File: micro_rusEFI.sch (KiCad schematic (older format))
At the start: 53 parts, among them J12 Conn_01x01, J13 Conn_01x01, J3 Conn_01x01, J4 Conn_02x05_Counter_Clockwise, J5 Conn_01x01, U3 molex_48pin_MRE, U7 XC6206 3.3V

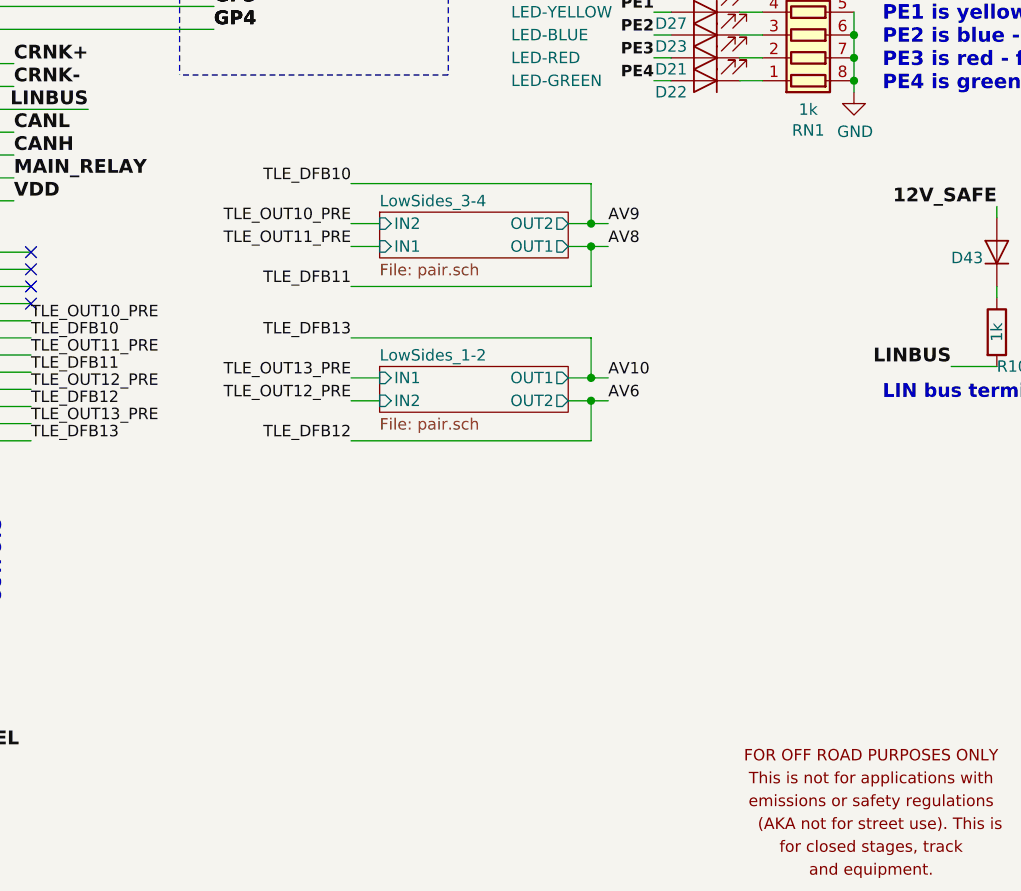
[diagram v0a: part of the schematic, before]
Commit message: AV6, AV8, AV9 and AV10 can now direct drive the digital outputs.
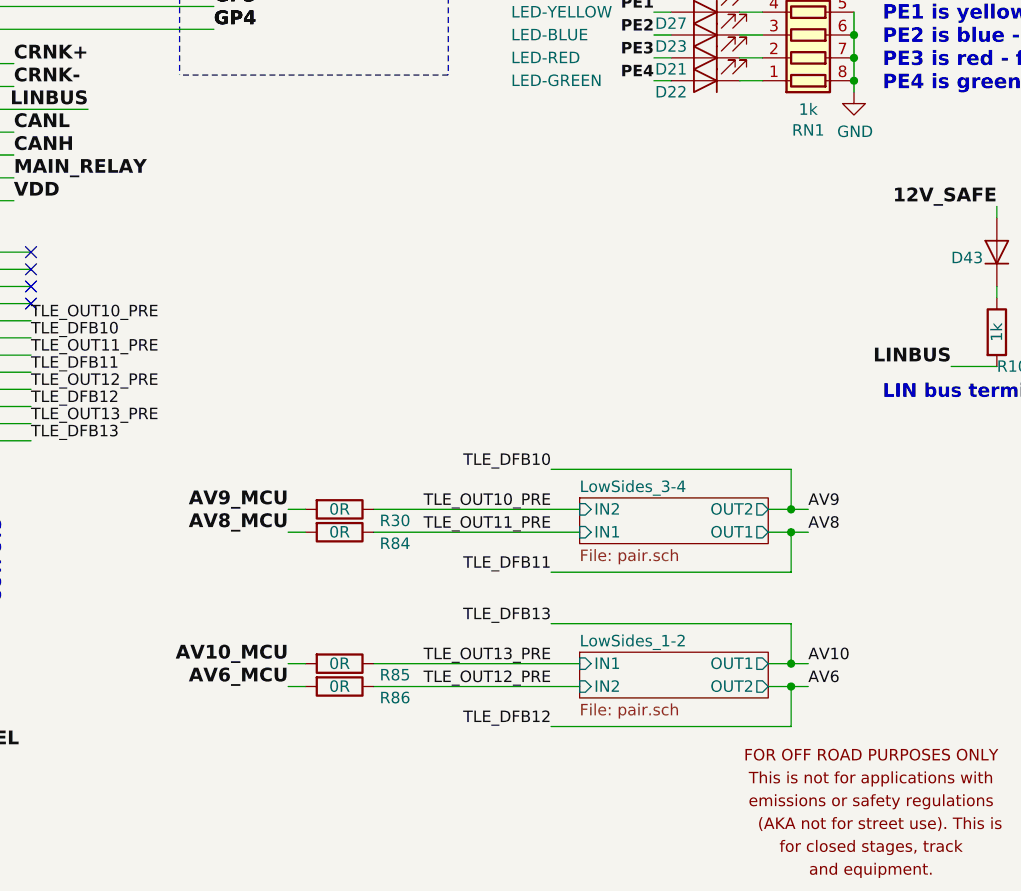
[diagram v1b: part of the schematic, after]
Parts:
- added R30, R84, R85: 0R, Resistor_SMD:R_0603_1608Metric, symbol Device:R
- added R86: 0R, Resistor_SMD:R_0805_2012Metric, symbol Device:R
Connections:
- net AV10_MCU: now also R85.2
- net AV6_MCU: now also R86.2
- net AV8_MCU: now also R84.2
- net AV9_MCU: now also R30.2
- net TLE_OUT10_PRE: now also R30.1
- net TLE_OUT11_PRE: now also R84.1
- net TLE_OUT12_PRE: now also R86.1
- net TLE_OUT13_PRE: now also R85.1
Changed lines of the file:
@@
 $EndComp
 $Sheet
-S 12450 6725 825  200
+S 13325 7975 825  200
 U 5E8F2073
 F0 "LowSides_3-4" 50
 F1 "pair.sch" 50
-F2 "IN1" I L 12450 6875 50
-F3 "IN2" I L 12450 6775 50
-F4 "OUT1" O R 13275 6875 50
-F5 "OUT2" O R 13275 6775 50
+F2 "IN1" I L 13325 8125 50
+F3 "IN2" I L 13325 8025 50
+F4 "OUT1" O R 14150 8125 50
+F5 "OUT2" O R 14150 8025 50
 $EndSheet
 $Sheet
-S 12450 7400 825  200
+S 13325 8650 825  200
 U 5E8F1149
 F0 "LowSides_1-2" 50
 F1 "pair.sch" 50
-F2 "IN1" I L 12450 7450 50
-F3 "IN2" I L 12450 7550 50
-F4 "OUT1" O R 13275 7450 50
-F5 "OUT2" O R 13275 7550 50
+F2 "IN1" I L 13325 8700 50
+F3 "IN2" I L 13325 8800 50
+F4 "OUT1" O R 14150 8700 50
+F5 "OUT2" O R 14150 8800 50
 $EndSheet
 Wire Wire Line
@@
 Wire Wire Line
 	10750 7500 10925 7500
-Text Label 12325 7550 2    50   ~ 0
+Text Label 13200 8800 2    50   ~ 0
 TLE_OUT12_PRE
 Text Label 8875 3400 2    50   ~ 0
@@
 Text Label 8875 3700 2    50   ~ 0
 PD15
-Wire Wire Line
-	12325 7550 12450 7550
-Wire Wire Line
-	12450 7450 12325 7450
-Wire Wire Line
-	12325 6775 12450 6775
-Wire Wire Line
-	12325 6875 12450 6875
 Wire Wire Line
 	7900 1650 7900 1575
@@
 Text Label 3425 4425 2    60   ~ 12
 AV6
-Text Label 13450 6775 0    50   ~ 0
+Text Label 14325 8025 0    50   ~ 0
 AV9
-Text Label 13450 6875 0    50   ~ 0
+Text Label 14325 8125 0    50   ~ 0
 AV8
-Text Label 13450 7450 0    50   ~ 0
+Text Label 14325 8700 0    50   ~ 0
 AV10
 Wire Wire Line
@@
 	3425 4725 4050 4725
 Wire Wire Line
-	13275 7450 13375 7450
-Wire Wire Line
-	13275 7550 13375 7550
-Wire Wire Line
-	13275 6775 13375 6775
-Wire Wire Line
-	13275 6875 13375 6875
+	14150 8700 14250 8700
+Wire Wire Line
+	14150 8800 14250 8800
+Wire Wire Line
+	14150 8025 14250 8025
+Wire Wire Line
+	14150 8125 14250 8125
 Wire Wire Line
 	10750 6975 10925 6975
 Wire Wire Line
-	12325 7725 13375 7725
-Wire Wire Line
-	13375 7725 13375 7550
-Connection ~ 13375 7550
-Wire Wire Line
-	13375 7550 13450 7550
-Text Label 13450 7550 0    50   ~ 0
+	13200 8975 14250 8975
+Wire Wire Line
+	14250 8975 14250 8800
+Connection ~ 14250 8800
+Wire Wire Line
+	14250 8800 14325 8800
+Text Label 14325 8800 0    50   ~ 0
 AV6
 Text Label 10925 7275 0    50   ~ 0
@@
 Wire Wire Line
 	10750 7725 10925 7725
-Text Label 12325 7725 2    50   ~ 0
+Text Label 13200 8975 2    50   ~ 0
 TLE_DFB12
 Wire Wire Line
-	12325 7275 13375 7275
-Wire Wire Line
-	13375 7275 13375 7450
-Connection ~ 13375 7450
-Wire Wire Line
-	13375 7450 13450 7450
-Wire Wire Line
-	12325 6600 13375 6600
-Wire Wire Line
-	13375 6600 13375 6775
-Connection ~ 13375 6775
-Wire Wire Line
-	13375 6775 13450 6775
-Wire Wire Line
-	12325 7050 13375 7050
-Wire Wire Line
-	13375 7050 13375 6875
-Connection ~ 13375 6875
-Wire Wire Line
-	13375 6875 13450 6875
-Text Label 12325 7275 2    50   ~ 0
+	13200 8525 14250 8525
+Wire Wire Line
+	14250 8525 14250 8700
+Connection ~ 14250 8700
+Wire Wire Line
+	14250 8700 14325 8700
+Wire Wire Line
+	13200 7850 14250 7850
+Wire Wire Line
+	14250 7850 14250 8025
+Connection ~ 14250 8025
+Wire Wire Line
+	14250 8025 14325 8025
+Wire Wire Line
+	13200 8300 14250 8300
+Wire Wire Line
+	14250 8300 14250 8125
+Connection ~ 14250 8125
+Wire Wire Line
+	14250 8125 14325 8125
+Text Label 13200 8525 2    50   ~ 0
 TLE_DFB13
-Text Label 12325 7450 2    50   ~ 0
+Text Label 13200 8700 2    50   ~ 0
 TLE_OUT13_PRE
 Wire Wire Line
@@
 Wire Wire Line
 	10750 7425 10925 7425
-Text Label 12325 6875 2    50   ~ 0
+Text Label 13200 8125 2    50   ~ 0
 TLE_OUT11_PRE
-Text Label 12325 7050 2    50   ~ 0
+Text Label 13200 8300 2    50   ~ 0
 TLE_DFB11
-Text Label 12325 6775 2    50   ~ 0
+Text Label 13200 8025 2    50   ~ 0
 TLE_OUT10_PRE
-Text Label 12325 6600 2    50   ~ 0
+Text Label 13200 7850 2    50   ~ 0
 TLE_DFB10
 Text Label 12125 3525 0    60   ~ 12
@@
 Wire Wire Line
 	6200 5600 6275 5600
+$Comp
+L Device:R R85
+U 1 1 5EE637EC
+P 12275 8700
+F 0 "R85" V 12325 8875 50  0000 L CNN
+F 1 "0R" V 12275 8700 50  0000 C CNN
+F 2 "Resistor_SMD:R_0603_1608Metric" V 12205 8700 50  0001 C CNN
+F 3 "~" H 12275 8700 50  0001 C CNN
+F 4 "Uniroyal Elec" H 3950 2775 50  0001 C CNN "Manufacturer"
+F 5 "0603WAF0000T5E" H 3950 2775 50  0001 C CNN "Part #"
+F 6 "" H 3950 2775 50  0001 C CNN "VEND"
+F 7 "" H 3950 2775 50  0001 C CNN "VEND#"
+F 8 "C21189" H 12275 8700 50  0001 C CNN "LCSC"
+	1    12275 8700
+	0    1    1    0
+$EndComp
+$Comp
+L Device:R R86
+U 1 1 5EEECFE7
+P 12275 8800
+F 0 "R86" V 12325 8975 50  0000 L CNN
+F 1 "0R" V 12275 8800 50  0000 C CNN
+F 2 "Resistor_SMD:R_0805_2012Metric" V 12205 8800 50  0001 C CNN
+F 3 "~" H 12275 8800 50  0001 C CNN
+F 4 "" H 3950 2875 50  0001 C CNN "Manufacturer"
+F 5 "" H 3950 2875 50  0001 C CNN "Part #"
+F 6 "" H 3950 2875 50  0001 C CNN "VEND"
+F 7 "" H 3950 2875 50  0001 C CNN "VEND#"
+F 8 "" H 12275 8800 50  0001 C CNN "LCSC"
+	1    12275 8800
+	0    1    1    0
+$EndComp
+$Comp
+L Device:R R30
+U 1 1 5EF0FADE
+P 12275 8025
+F 0 "R30" V 12325 8200 50  0000 L CNN
+F 1 "0R" V 12275 8025 50  0000 C CNN
+F 2 "Resistor_SMD:R_0603_1608Metric" V 12205 8025 50  0001 C CNN
+F 3 "~" H 12275 8025 50  0001 C CNN
+F 4 "Uniroyal Elec" H 3950 2100 50  0001 C CNN "Manufacturer"
+F 5 "0603WAF0000T5E" H 3950 2100 50  0001 C CNN "Part #"
+F 6 "" H 3950 2100 50  0001 C CNN "VEND"
+F 7 "" H 3950 2100 50  0001 C CNN "VEND#"
+F 8 "C21189" H 12275 8025 50  0001 C CNN "LCSC"
+	1    12275 8025
+	0    1    1    0
+$EndComp
+$Comp
+L Device:R R84
+U 1 1 5EF0FAED
+P 12275 8125
+F 0 "R84" V 12325 8300 50  0000 L CNN
+F 1 "0R" V 12275 8125 50  0000 C CNN
+F 2 "Resistor_SMD:R_0603_1608Metric" V 12205 8125 50  0001 C CNN
+F 3 "~" H 12275 8125 50  0001 C CNN
+F 4 "Uniroyal Elec" H 3950 2200 50  0001 C CNN "Manufacturer"
+F 5 "0603WAF0000T5E" H 3950 2200 50  0001 C CNN "Part #"
+F 6 "" H 3950 2200 50  0001 C CNN "VEND"
+F 7 "" H 3950 2200 50  0001 C CNN "VEND#"
+F 8 "C21189" H 12275 8125 50  0001 C CNN "LCSC"
+	1    12275 8125
+	0    1    1    0
+$EndComp
+Text Label 12050 8025 2    60   ~ 12
+AV9_MCU
+Text Label 12050 8125 2    60   ~ 12
+AV8_MCU
+Text Label 12050 8700 2    60   ~ 12
+AV10_MCU
+Text Label 12050 8800 2    60   ~ 12
+AV6_MCU
+Wire Wire Line
+	12050 8025 12125 8025
+Wire Wire Line
+	12050 8125 12125 8125
+Wire Wire Line
+	12050 8700 12125 8700
+Wire Wire Line
+	12050 8800 12125 8800
+Wire Wire Line
+	12425 8700 13325 8700
+Wire Wire Line
+	12425 8800 13325 8800
+Wire Wire Line
+	12425 8025 13325 8025
+Wire Wire Line
+	12425 8125 13325 8125
 $EndSCHEMATC

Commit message: 0.5.1 released
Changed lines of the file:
@@
 F19 "AV3_MCU" I R 5600 4125 60
 F20 "AV5_MCU" I R 5600 4325 60
-F21 "12V-SWITCH" I L 4050 5150 60
-F22 "Vbat_MCU" I R 5600 5150 60
-F23 "AV6" I L 4050 4425 60
-F24 "AV7" I L 4050 4525 60
-F25 "AV8" I L 4050 4625 60
-F26 "AV9" I L 4050 4725 60
-F27 "AV6_MCU" I R 5600 4425 60
-F28 "AV7_MCU" I R 5600 4525 60
-F29 "AV8_MCU" I R 5600 4625 60
-F30 "AV9_MCU" I R 5600 4725 60
-F31 "CAM" I L 4050 5000 60
-F32 "CAM_MCU" I R 5600 5000 60
-F33 "AV4" I L 4050 4225 60
-F34 "AV4_MCU" I R 5600 4225 60
-F35 "AGND" I R 5600 5400 50
-F36 "AV11_MCU" I R 5600 5275 50
+F21 "Vbat_MCU" I R 5600 5150 60
+F22 "AV6" I L 4050 4425 60
+F23 "AV7" I L 4050 4525 60
+F24 "AV8" I L 4050 4625 60
+F25 "AV9" I L 4050 4725 60
+F26 "AV6_MCU" I R 5600 4425 60
+F27 "AV7_MCU" I R 5600 4525 60
+F28 "AV8_MCU" I R 5600 4625 60
+F29 "AV9_MCU" I R 5600 4725 60
+F30 "CAM" I L 4050 5000 60
+F31 "CAM_MCU" I R 5600 5000 60
+F32 "AV4" I L 4050 4225 60
+F33 "AV4_MCU" I R 5600 4225 60
+F34 "AGND" I R 5600 5400 50
+F35 "AV11_MCU" I R 5600 5275 50
+F36 "12V" I L 4050 5150 50
 $EndSheet
 Text Label 3425 4425 2    60   ~ 12

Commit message: 0.5.1 released
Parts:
- R85: LCSC C21189 -> (none)
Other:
- note added: "NOT OEM POPULATED\nOEM IS \nAV6 AND AV10 ARE ANALOG\nAV8 AND AV9 ARE DIGITAL OUTPUTS"
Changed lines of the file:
@@
 F 6 "" H 3950 2775 50  0001 C CNN "VEND"
 F 7 "" H 3950 2775 50  0001 C CNN "VEND#"
-F 8 "C21189" H 12275 8700 50  0001 C CNN "LCSC"
+F 8 "" H 12275 8700 50  0001 C CNN "LCSC"
 	1    12275 8700
 	0    1    1    0
@@
 Wire Wire Line
 	12425 8125 13325 8125
+Wire Notes Line
+	12125 8625 12125 8875
+Wire Notes Line
+	12125 8875 12425 8875
+Wire Notes Line
+	12425 8875 12425 8625
+Wire Notes Line
+	12425 8625 12125 8625
+Text Notes 11325 9300 0    50   ~ 0
+NOT OEM POPULATED\nOEM IS \nAV6 AND AV10 ARE ANALOG\nAV8 AND AV9 ARE DIGITAL OUTPUTS
+Wire Notes Line
+	12275 8875 12125 9000
 $EndSCHEMATC

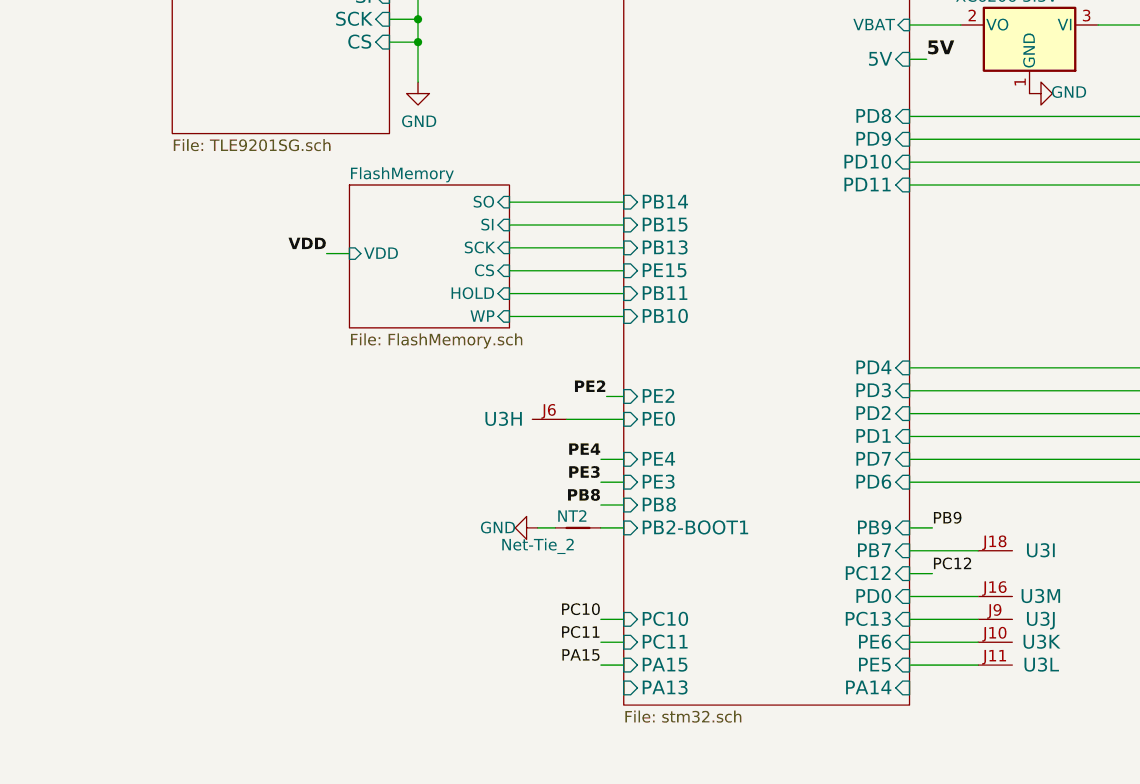
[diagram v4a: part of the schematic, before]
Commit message: R0.5.2 drafted per https://github.com/rusefi/hw_microRusEfi/issues/180
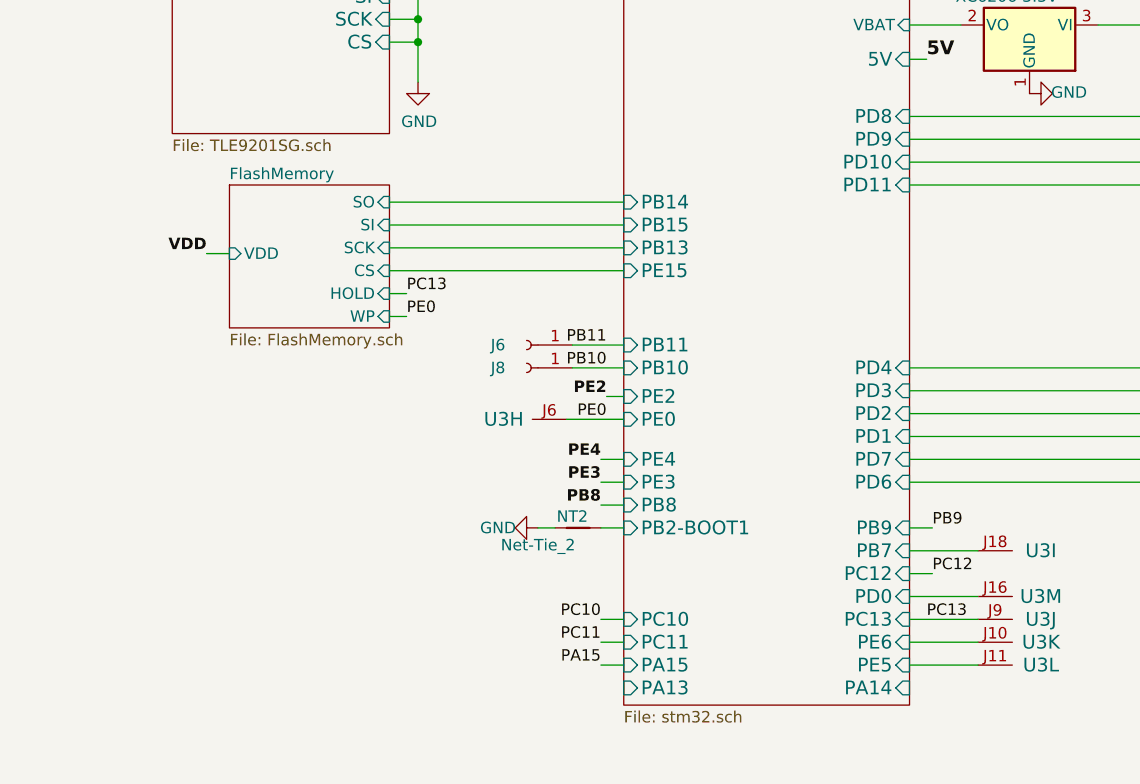
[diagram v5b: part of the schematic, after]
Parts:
- added J6, J8: Conn_01x01_Female, Connector_PinHeader_1.00mm:PinHeader_1x01_P1.00mm_Vertical, symbol Connector:Conn_01x01_Female
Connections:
- net MCU/PC13 renamed PC13
- net MCU/PE0 renamed PE0
- new net PB10: J8.1 (Pin_1)
- new net PB11: J6.1 (Pin_1)
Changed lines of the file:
@@
 $EndComp
 $Sheet
-S 5500 7325 700  625
+S 4975 7325 700  625
 U 5D2F23B4
 F0 "FlashMemory" 50
 F1 "FlashMemory.sch" 50
-F2 "SI" I R 6200 7500 50
-F3 "SCK" I R 6200 7600 50
-F4 "CS" I R 6200 7700 50
-F5 "SO" I R 6200 7400 50
-F6 "VDD" I L 5500 7625 50
-F7 "HOLD" I R 6200 7800 50
-F8 "WP" I R 6200 7900 50
+F2 "SI" I R 5675 7500 50
+F3 "SCK" I R 5675 7600 50
+F4 "CS" I R 5675 7700 50
+F5 "SO" I R 5675 7400 50
+F6 "VDD" I L 4975 7625 50
+F7 "HOLD" I R 5675 7800 50
+F8 "WP" I R 5675 7900 50
 $EndSheet
-Text Label 5400 7625 2    50   ~ 10
+Text Label 4875 7625 2    50   ~ 10
 VDD
 $Comp
@@
 $EndComp
 Wire Wire Line
-	6200 7400 6700 7400
-Wire Wire Line
-	6700 7500 6200 7500
-Wire Wire Line
-	6200 7600 6700 7600
-Wire Wire Line
-	6700 7700 6200 7700
-Wire Wire Line
-	6700 7900 6200 7900
-Wire Wire Line
-	6200 7800 6700 7800
+	5675 7400 6700 7400
+Wire Wire Line
+	6700 7500 5675 7500
+Wire Wire Line
+	5675 7600 6700 7600
+Wire Wire Line
+	6700 7700 5675 7700
 $Comp
 L power:GND #PWR0214
@@
 F14 "PE13" I R 7950 3925 60
 F15 "PE15" I L 6700 7700 60
-F16 "PB11" I L 6700 7800 60
+F16 "PB11" I L 6700 8025 60
 F17 "PB13" I L 6700 7600 60
 F18 "PB15" I L 6700 7500 60
@@
 F33 "PE12" I R 7950 4025 60
 F34 "PE14" I R 7950 3825 60
-F35 "PB10" I L 6700 7900 60
+F35 "PB10" I L 6700 8125 60
 F36 "PB12" I R 7950 4925 60
 F37 "PB14" I L 6700 7400 60
@@
 	6325 8825 6400 8825
 Wire Wire Line
-	5400 7625 5500 7625
+	4875 7625 4975 7625
 Wire Wire Line
 	4650 6225 4725 6225
@@
 Wire Notes Line
 	12275 8875 12125 9000
+Text Label 6625 8350 2    50   ~ 0
+PE0
+Text Label 8025 9225 0    50   ~ 0
+PC13
+Text Label 5750 7900 0    50   ~ 0
+PE0
+Text Label 5750 7800 0    50   ~ 0
+PC13
+Wire Wire Line
+	5675 7800 5750 7800
+Wire Wire Line
+	5675 7900 5750 7900
+$Comp
+L Connector:Conn_01x01_Female J6
+U 1 1 5F134DAE
+P 6275 8025
+F 0 "J6" H 6400 8025 50  0000 C CNN
+F 1 "Conn_01x01_Female" H 6167 7891 50  0001 C CNN
+F 2 "Connector_PinHeader_1.00mm:PinHeader_1x01_P1.00mm_Vertical" H 6275 8025 50  0001 C CNN
+F 3 "~" H 6275 8025 50  0001 C CNN
+	1    6275 8025
+	-1   0    0    1
+$EndComp
+$Comp
+L Connector:Conn_01x01_Female J8
+U 1 1 5F199C4D
+P 6275 8125
+F 0 "J8" H 6400 8125 50  0000 C CNN
+F 1 "Conn_01x01_Female" H 6167 7991 50  0001 C CNN
+F 2 "Connector_PinHeader_1.00mm:PinHeader_1x01_P1.00mm_Vertical" H 6275 8125 50  0001 C CNN
+F 3 "~" H 6275 8125 50  0001 C CNN
+	1    6275 8125
+	-1   0    0    1
+$EndComp
+Wire Wire Line
+	6700 8025 6475 8025
+Wire Wire Line
+	6700 8125 6475 8125
+Text Label 6625 8125 2    50   ~ 0
+PB10
+Text Label 6625 8025 2    50   ~ 0
+PB11
 $EndSCHEMATC
